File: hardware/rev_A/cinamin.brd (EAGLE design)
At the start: 16.1 x 8.6 mm, 11 parts, among them U1 AP4400_3.4_2.3, X1 16Mhz

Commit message: prototype board mostly done, clean up board and schematic before ordering tonight
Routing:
- net GND: vias 9 -> 7
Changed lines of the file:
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@@
 <via x="3.65" y="3.55" extent="1-16" drill="0.1016" diameter="0.3048"/>
 <via x="3.65" y="2.75" extent="1-16" drill="0.1016" diameter="0.3048"/>
-<via x="2.85" y="3.95" extent="1-16" drill="0.1016" diameter="0.3048"/>
-<via x="2.45" y="3.55" extent="1-16" drill="0.1016" diameter="0.3048"/>
 <polygon width="0.01" layer="16" isolate="0.1016" thermals="no">
 <vertex x="0" y="0"/>
@@
 <wire x1="5.15" y1="7.8" x2="6.25" y2="7.8" width="0.1016" layer="1"/>
 <wire x1="0.46" y1="1.583" x2="-4.833" y2="5.2762" width="0" layer="19" extent="1-16"/>
+<wire x1="2.062" y1="3.542" x2="3.65" y2="3.55" width="0" layer="19" extent="1-1"/>
 </signal>
 <signal name="SW_CLK">

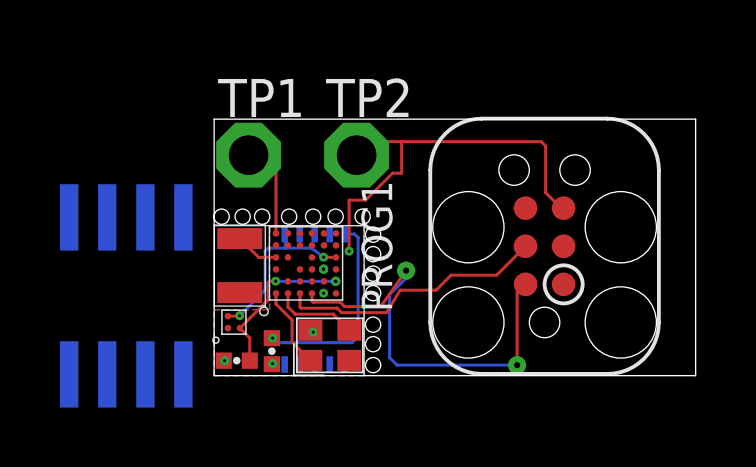
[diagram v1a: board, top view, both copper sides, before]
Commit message: cleaned up some traces, changed to 0603 cap
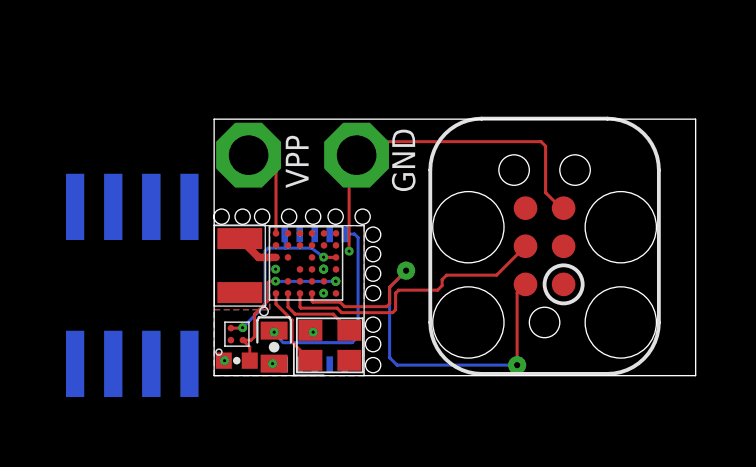
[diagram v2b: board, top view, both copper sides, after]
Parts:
- C1: value 15uF -> 47uF; device passives:0402_CAP -> passives:0603_CAP_SMALL
- U$4: value (none) -> LD391151.4V
- moved U$4 0.41 mm to (0.76, 1.38)
- moved D1 0.40 mm to (-2.73, 3.01)
- moved C1 0.15 mm to (2.00, 0.95)
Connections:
- net GND: now also C1.NEG; no longer C1.2
- net N$3: now also C1.POS; no longer C1.1
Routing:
- net GND: track 13.8 -> 12.2 mm, vias 7 -> 8
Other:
- board text added: "GND"
- board text added: "VPP"

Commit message: changed the revand the new prototype to include the transistor switch
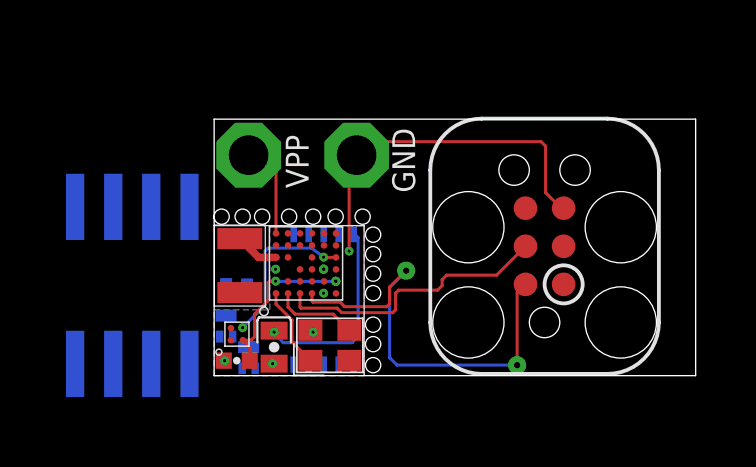
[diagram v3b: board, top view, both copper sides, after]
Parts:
- added Q1, Q2: (no value), fets:XFDFN-3
- added Q3: MOSFET-NCHANNELXFDN-3, fets:XFDFN-3
- moved U1 0.30 mm to (3.65, 2.57)
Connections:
- new net N$2: Q1.G, Q3.G, U1.6
- new net N$4: Q1.D, Q2.G, Q3.D
- net GND: now also Q3.S
- net N$3: now also Q1.S, Q2.S
- net VCC: now also Q2.D; no longer U1.6
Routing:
- net VCC: track 6.26 -> 5.38 mm
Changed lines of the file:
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@@
 <attribute name="VALUE" x="0.755" y="1.897" size="1.016" layer="27" font="vector" ratio="12" rot="R180" align="bottom-center"/>
 </element>
-<element name="U1" library="chips" package="TSOP-10" value="AP4400_3.4_2.3" x="3.352" y="2.57" smashed="yes" rot="MR0">
-<attribute name="DIGIKEY" value="CANT_BUY" x="3.352" y="2.57" size="1.778" layer="28" rot="MR0" display="off"/>
-<attribute name="VALUE" x="-0.458" y="1.3" size="1.016" layer="28" rot="MR90"/>
+<element name="U1" library="chips" package="TSOP-10" value="AP4400_3.4_2.3" x="3.652" y="2.57" smashed="yes" rot="MR0">
+<attribute name="DIGIKEY" value="CANT_BUY" x="3.652" y="2.57" size="1.778" layer="28" rot="MR0" display="off"/>
+<attribute name="VALUE" x="-0.158" y="1.3" size="1.016" layer="28" rot="MR90"/>
 </element>
 <element name="TP1" library="testpad" package="P1-13" value="TPSPAD1-13" x="1.15" y="7.35" smashed="yes">
@@
 </element>
 <element name="C1" library="passives" package="0603_CAP_SMALL" value="47uF" x="2" y="0.95" smashed="yes" rot="R270"/>
+<element name="Q1" library="fets" package="XFDFN-3" value="" x="1.15" y="0.6" smashed="yes" rot="MR90">
+<attribute name="DIGIKEY" value="DMP21D5UFB4-7BDICT-ND" x="1.15" y="0.6" size="1.778" layer="28" rot="MR90" display="off"/>
+<attribute name="VALUE" x="-0.35" y="0.6" size="1.016" layer="28" font="vector" ratio="12" rot="MR90" align="bottom-center"/>
+</element>
+<element name="Q2" library="fets" package="XFDFN-3" value="" x="0.4" y="1.65" smashed="yes" rot="MR90">
+<attribute name="DIGIKEY" value="DMP21D5UFB4-7BDICT-ND" x="0.4" y="1.65" size="1.778" layer="28" rot="MR90" display="off"/>
+<attribute name="VALUE" x="-1.1" y="1.65" size="1.016" layer="28" font="vector" ratio="12" rot="MR90" align="bottom-center"/>
+</element>
+<element name="Q3" library="fets" package="XFDFN-3" value="MOSFET-NCHANNELXFDN-3" x="0.75" y="2.9" smashed="yes" rot="MR0">
+<attribute name="DIGIKEY" value="DMN2400UFB4-7DICT-ND" x="0.75" y="2.9" size="1.778" layer="28" rot="MR0" display="off"/>
+<attribute name="VALUE" x="0.75" y="1.4" size="1.016" layer="28" font="vector" ratio="12" rot="MR0" align="bottom-center"/>
+</element>
 </elements>
 <signals>
@@
 <wire x1="4.75" y1="7.35" x2="5.2" y2="7.8" width="0.1016" layer="1"/>
 <wire x1="5.2" y1="7.8" x2="10.9" y2="7.8" width="0.1016" layer="1"/>
+<contactref element="Q3" pad="S"/>
 <wire x1="0.56" y1="1.183" x2="-4.633" y2="5.6262" width="0" layer="19" extent="1-16"/>
+<wire x1="1.1" y1="2.685" x2="2" y2="0.4" width="0" layer="19" extent="1-1"/>
 </signal>
 <signal name="SW_CLK">
@@
 </signal>
 <signal name="VCC">
-<contactref element="U1" pad="6"/>
-<contactref element="U$4" pad="B2"/>
-<contactref element="U$4" pad="A2"/>
 <contactref element="U$3" pad="F4"/>
 <contactref element="U$3" pad="E4"/>
 <wire x1="4.062" y1="3.942" x2="3.662" y2="3.942" width="0.1016" layer="1"/>
-<wire x1="0.56" y1="1.583" x2="0.96" y2="1.583" width="0.1016" layer="1"/>
 <via x="3.65" y="3.95" extent="1-16" drill="0.1016" diameter="0.3048"/>
 <wire x1="3.65" y1="3.95" x2="3.25" y2="4.25" width="0.1016" layer="16"/>
-<wire x1="3.25" y1="4.25" x2="2.372" y2="4.25" width="0.1016" layer="16"/>
-<wire x1="2.372" y1="4.25" x2="2.352" y2="4.72" width="0.1016" layer="16"/>
+<wire x1="3.25" y1="4.25" x2="1.8" y2="4.25" width="0.1016" layer="16"/>
 <wire x1="3.662" y1="3.942" x2="3.658" y2="3.942" width="0.1016" layer="1"/>
 <wire x1="3.658" y1="3.942" x2="3.65" y2="3.95" width="0.1016" layer="1"/>
 <via x="0.95" y="1.6" extent="1-16" drill="0.1016" diameter="0.3048"/>
-<wire x1="0.96" y1="1.583" x2="0.96" y2="1.59" width="0.1016" layer="1"/>
 <wire x1="0.96" y1="1.59" x2="0.95" y2="1.6" width="0.1016" layer="1"/>
-<wire x1="2.372" y1="4.25" x2="1.8" y2="4.25" width="0.1016" layer="16"/>
 <wire x1="1.8" y1="4.25" x2="1.7" y2="4.15" width="0.1016" layer="16"/>
 <wire x1="1.7" y1="4.15" x2="1.7" y2="2.35" width="0.1016" layer="16"/>
 <wire x1="1.7" y1="2.35" x2="0.95" y2="1.6" width="0.1016" layer="16"/>
+<contactref element="U$4" pad="A2"/>
+<contactref element="U$4" pad="B2"/>
+<contactref element="Q2" pad="D"/>
+<wire x1="0.96" y1="1.583" x2="0.96" y2="1.59" width="0" layer="19" extent="1-1"/>
+<wire x1="0.56" y1="1.583" x2="0.96" y2="1.59" width="0" layer="19" extent="1-1"/>
+<wire x1="0.4" y1="2" x2="0.56" y2="1.583" width="0" layer="19" extent="1-1"/>
 </signal>
 <signal name="N$3">
@@
 <via x="2" y="1.45" extent="1-16" drill="0.1016" diameter="0.3048"/>
 <wire x1="2.00093125" y1="1.54906875" x2="2" y2="1.45" width="0.1016" layer="1"/>
-<wire x1="4.352" y1="4.72" x2="4.68" y2="4.72" width="0.1016" layer="16"/>
+<wire x1="4.652" y1="4.72" x2="4.68" y2="4.72" width="0.1016" layer="16"/>
 <wire x1="4.68" y1="4.72" x2="4.8" y2="4.6" width="0.1016" layer="16"/>
 <wire x1="4.8" y1="4.6" x2="4.8" y2="1.3" width="0.1016" layer="16"/>
@@
 <wire x1="2.00093125" y1="1.54906875" x2="2.00093125" y2="1.50093125" width="0.1016" layer="1"/>
 <wire x1="2.00093125" y1="1.50093125" x2="2" y2="1.5" width="0.1016" layer="1"/>
+<contactref element="Q1" pad="S"/>
+<contactref element="Q2" pad="S"/>
 <wire x1="2.00093125" y1="1.54906875" x2="-0.823" y2="5.6262" width="0" layer="19" extent="1-16"/>
+<wire x1="0.935" y1="0.25" x2="2.3" y2="1.1" width="0" layer="19" extent="1-16"/>
+<wire x1="0.185" y1="1.3" x2="0.935" y2="0.25" width="0" layer="19" extent="1-1"/>
 </signal>
 <signal name="OUT">
@@
 <wire x1="2.062" y1="6.788" x2="1.15" y2="7.35" width="0.1016" layer="1"/>
 </signal>
+<signal name="N$2">
+<contactref element="U1" pad="6"/>
+<contactref element="Q1" pad="G"/>
+<contactref element="Q3" pad="G"/>
+<wire x1="1.365" y1="0.25" x2="2.652" y2="4.72" width="0" layer="19" extent="1-16"/>
+<wire x1="1.1" y1="3.115" x2="1.365" y2="0.25" width="0" layer="19" extent="1-1"/>
+</signal>
+<signal name="N$4">
+<contactref element="Q1" pad="D"/>
+<contactref element="Q3" pad="D"/>
+<contactref element="Q2" pad="G"/>
+<wire x1="1.15" y1="0.95" x2="0.4" y2="2.9" width="0" layer="19" extent="1-1"/>
+<wire x1="0.615" y1="1.3" x2="1.15" y2="0.95" width="0" layer="19" extent="1-1"/>
+</signal>
 </signals>
